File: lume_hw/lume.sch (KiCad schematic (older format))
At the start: 76 parts, among them SW1 BUTTON, SW2 BUTTON, SW3 BUTTON

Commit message: + Lume3 sent to production
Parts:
- removed DA1: AAT3221, symbol AAT3221
- removed DA2: NCP662SQ, symbol NCP662SQ
- removed DD1, DD3: PCA9635, symbol PCA9635
- removed DD2: STM32F100C4, symbol STM32F100C4
- removed FU1, FU2, FU3, FU4: SOLDERFUSE, symbol SOLDERFUSE
- removed HOLE1, HOLE2, HOLE3, HOLE4: HOLE_METALLED, symbol HOLE_METALLED-RESCUE-lume2
- removed R10, R11, R12, R13, R14, R15, R16, R17, R18, R19, R20, R21, R22, R23, R24, R25, R26, R27, R28, R29, R30, R31, R33, R4, R5, R6, R7, R8, R9: 100R, RES_0603, symbol R
- removed R32, R34: 4k7, RES_0603, symbol R
- removed XL1: CONN_3, symbol CONN_3
- removed XL10: CONN_1, symbol CONN_1
- removed XL2, XL4, XL5, XL6, XL7: CONN_10, symbol CONN_10
- removed XL9: USB_MINI_B, symbol USB_MINI_B
- added C14: 0.1u, Capacitors:CAP_0603, symbol C
- added DA1: NCP583SQ, SOT:SC82AB, symbol NCP583SQ
- added DA2: MCP1700, SOT:SOT23-3, symbol MCP1700
- added DA3: MC74VHC1, SOT:SOT23-5, symbol MC74VHC1
- added DD1: STM32F072CxTx, LQFP_TQFP:LQFP48, symbol STM32F072CxTx
- added HOLE1, HOLE2, HOLE3, HOLE4: HOLE_METALLED, PCB:Hole3_5_out6mm, symbol HOLE_METALLED
- added Logo1: Logo, Pictures:Ostranna_12d7_10d1, symbol Logo
- added Q1: ALS-PT19-315C, Resistors:RES_0603, symbol Phototransistor
- added SW4: BUTTON, BtnsSwitches:BTN_6x6_4x4, symbol BUTTON
- added TP1, TP2: TESTPOINT, PCB:TESTPOINT_1MM, symbol TESTPOINT
- added XL1: USB_MINI_B, Connectors:USBmicro_MOLEX_1050170001, symbol USB_MINI_B
- added XL2: CONN_6, Connectors:PLS-6, symbol CONN_6
- added XL4: CONN_3, Connectors:SLD_3_2D5, symbol CONN_3
- added XTAL2: 12MHz, Quartz:0503x4-4, symbol CRYSTAL_H
- B1: footprint CR2032 -> Installation:BATTERY_CH7410
- C1: value 4.7u -> 10n; footprint CAP_0603 -> Capacitors:CAP_0603
- C10: value 4.7u -> 6.8pF; footprint CAP_0603 -> Capacitors:CAP_0603; Price (none) -> 0.5; SolderPoints (none) -> 2
- C11: value 0.1u -> 18pF; footprint CAP_0603 -> Capacitors:CAP_0603; Price (none) -> 0.5; SolderPoints (none) -> 2
- C12: value 1u -> 18pF; footprint CAP_0603 -> Capacitors:CAP_0603; Price (none) -> 0.5; SolderPoints (none) -> 2
- C13: value 1u -> 0.1u; footprint CAP_0603 -> Capacitors:CAP_0603
- C2, C5: value 0.1u -> 1u; footprint CAP_0603 -> Capacitors:CAP_0603
- C3, C4, C9: footprint CAP_0603 -> Capacitors:CAP_0603; Price (none) -> 0.5; SolderPoints (none) -> 2
- C6: value 4.7u -> 0.1u; footprint CAP_0603 -> Capacitors:CAP_0603; Price (none) -> 0.5; SolderPoints (none) -> 2
- C7: value 1u -> 10u; footprint CAP_0603 -> Capacitors:CAP_0603; Price (none) -> 0.5; SolderPoints (none) -> 2
- C8: value 6.8pF -> 1u; footprint CAP_0603 -> Capacitors:CAP_0603; Price (none) -> 0.5; SolderPoints (none) -> 2
- D1: value SS14 -> PMEG2020; footprint SMA -> Diodes:SOD323; Price (none) -> 5; SolderPoints (none) -> 2
- R1: value 100R -> 1k; footprint RES_0603 -> Resistors:RES_0603; Price (none) -> 0.5; SolderPoints (none) -> 2
- R2: value 100R -> 10k; footprint RES_0603 -> Resistors:RES_0603; Price (none) -> 0.5; SolderPoints (none) -> 2
- R3: footprint RES_0603 -> Resistors:RES_0603; Price (none) -> 0.5; SolderPoints (none) -> 2
- SW1, SW2, SW3: footprint (none) -> BtnsSwitches:BTN_6x6_4x4; Price (none) -> 1; SolderPoints (none) -> 4
- XL3: footprint (none) -> Connectors:NOKIA_10PIN
- XL8: footprint (none) -> Connectors:SLD_2_2D5
- XTAL1: footprint (none) -> Quartz:KX26
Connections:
- net +3.3V: now also C8.1, DA1.3 (Vout), DA2.2 (OUT), DD1.24 (VDD), DD1.36 (VDD), DD1.48 (VDD), DD1.9 (VDDA), Q1.1 (C), XL2.1; no longer C1.1, C10.1, C11.1, C13.1, C2.1
- net +5V: now also C1.2, C2.1, C14.1, DA1.1 (EN), DA1.4 (Vin), DA2.3 (IN), DA3.5 (Vcc), XL1.1 (UVcc), XL4.1 (P1); no longer C12.1
- net Btn1: now also DD1.39 (PB3/T2C2/SCK1)
- net Btn2: now also DD1.40 (PB4/T3C1/MISO1)
- net Btn3: now also DD1.41 (PB5/T3C2/MOSI1)
- net GND: now also C1.1, R2.2, XL8.1 (P1), C14.2, DA1.2 (GND), DA2.1 (GND), DA3.1 (~OE), DA3.3 (GND), DD1.23 (VSS), DD1.35 (VSS), DD1.44 (BOOT0), DD1.47 (VSS), DD1.8 (VSSA), HOLE1.H, HOLE2.H, HOLE3.H, HOLE4.H, SW4.1, XL1.4 (UID), XL1.5 (UGND), XL2.3, XL4.3, XTAL2.H; no longer C1.2, XL8.2 (PM)
- net LCD_BCKLT: now also R3.1, DD1.27 (PB14/MISO2/SDA2/T1C2N/T15C1); no longer XL3.6 (LED+)
- net LCD_SCLK: now also DD1.25 (PB12/CK3)
- net LCD_SDA: now also DD1.21 (PB10/SCK2/SCL2/TX3/T2C3)
- net LCD_XCS: now also DD1.26 (PB13/SCK2/SCL2/T1C1N)
- net LCD_XRES: now also DD1.22 (PB11/SDA2/RX3/T2C4)
- net SWCLK: now also DD1.37 (TX2/SWCLK/PA14), XL2.2
- net SWDIO: now also DD1.34 (IROUT/USBNOE/SWDIO/PA13), XL2.4
- net at XTAL1.1: now also C10.1, DD1.3 (OC32IN/PC14); no longer C9.1
- net at XTAL1.2: now also C9.1, DD1.4 (OC32OUT/PC15); no longer C8.1
- net at B1.A: now also DD1.1 (VBat)
- net at R1.1: now also C11.1, XTAL2.2
- net LUM_MEAS: now reaches R2.1
- net LUM_MEAS: now also C13.1, DD1.11 (ADC1/RX4/T15C1N/T2C2/PA1), Q1.2 (E)
- net at R1.2: now also DD1.6 (OSCOUT/PF1)
- net at R3.2: now also XL3.6 (LED+)
- net at D1.A: now also XL8.2 (PM); no longer XL8.1 (P1)
- new net: DA3.4 (OutY), XL4.2 (PM)
- new net: C12.1, DD1.5 (OSCIN/PF0), XTAL2.1
- new net Btn4: DD1.42 (PB6/SCL1/T16C1N/TX1), SW4.2
- new net D+: DD1.33 (T1ETR/USBDP/PA12), XL1.3 (D+)
- new net D-: DD1.32 (T1C4/USBDM/PA11), XL1.2 (D-)
- new net MCO: DD1.29 (MCO/CK1/T1C1/PA8), TP1.1
- new net UART_RX: DD1.31 (T1C3/RX1/PA10), XL2.6
- new net UART_TX: DD1.30 (T1C2/TX1/PA9), XL2.5
- new net WS_CTRL: DA3.2 (InA), DD1.28 (PB15/MOSI2/T1C3N/T15C1N/T15C2), TP2.1
- no-connect marks 16 -> 20
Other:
- note added: "One or another"
- note added: "Programming & debug"
- note removed: "3.3V 150mA power regulator"
- note removed: "Address\nsetting"
- note removed: "LEDs controller\nI2C addr = 0x1A"
- note removed: "LEDs controller\nI2C addr = 0x2B"
- moved on the sheet: XL3, XTAL1

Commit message: proceeding
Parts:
- removed C11, C12: 18pF, Capacitors:CAP_0603, symbol C
- removed R1: 1k, Resistors:RES_0603, symbol R
- removed XTAL2: 12MHz, Quartz:0503x4-4, symbol CRYSTAL_H
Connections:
- no-connect marks 20 -> 22
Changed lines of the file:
@@
 	5900 3100 6350 3100
-$Comp
-L CONN_3 XL4
-U 1 1 59A0593F
-P 14700 3800
-F 0 "XL4" V 14650 3800 40  0000 C CNN
-F 1 "CONN_3" V 14750 3800 40  0000 C CNN
-F 2 "Connectors:SLD_3_2D5" V 14550 3700 60  0001 C CNN
-F 3 "" V 14650 3800 60  0001 C CNN
-F 4 "1" V 14750 3900 60  0001 C CNN "Price"
-F 5 "3" V 14850 4000 60  0001 C CNN "SolderPoints"
-	1    14700 3800
-	-1   0    0    -1
-$EndComp
 $Comp
 L +5V #PWR029
@@
 $EndComp
 NoConn ~ 9600 3500
-$Comp
-L GND #PWR020
-U 1 1 59A128EC
-P 10850 4800
-F 0 "#PWR020" H 10940 4780 30  0001 C CNN
-F 1 "GND" H 10850 4720 30  0001 C CNN
-F 2 "" H 10850 4800 60  0001 C CNN
-F 3 "" H 10850 4800 60  0001 C CNN
-	1    10850 4800
-	-1   0    0    -1
-$EndComp
-$Comp
-L GND #PWR022
-U 1 1 59A128F2
-P 11050 4800
-F 0 "#PWR022" H 11140 4780 30  0001 C CNN
-F 1 "GND" H 11050 4720 30  0001 C CNN
-F 2 "" H 11050 4800 60  0001 C CNN
-F 3 "" H 11050 4800 60  0001 C CNN
-	1    11050 4800
-	-1   0    0    -1
-$EndComp
-$Comp
-L GND #PWR019
-U 1 1 59A128F8
-P 10650 4800
-F 0 "#PWR019" H 10740 4780 30  0001 C CNN
-F 1 "GND" H 10650 4720 30  0001 C CNN
-F 2 "" H 10650 4800 60  0001 C CNN
-F 3 "" H 10650 4800 60  0001 C CNN
-	1    10650 4800
-	-1   0    0    -1
-$EndComp
-$Comp
-L R R1
-U 1 1 59A12900
-P 10650 3900
-F 0 "R1" V 10730 3750 50  0000 C CNN
-F 1 "1k" V 10650 3900 50  0000 C CNN
-F 2 "Resistors:RES_0603" V 10730 4000 28  0001 C CNN
-F 3 "" V 10730 3750 60  0000 C CNN
-F 4 "0.5" V 10830 3850 60  0001 C CNN "Price"
-F 5 "2" V 10930 3950 60  0001 C CNN "SolderPoints"
-	1    10650 3900
-	1    0    0    1
-$EndComp
-$Comp
-L CRYSTAL_H XTAL2
-U 1 1 59A12909
-P 10850 4250
-F 0 "XTAL2" V 10750 4500 60  0000 C CNN
-F 1 "12MHz" V 10850 4500 60  0000 C CNN
-F 2 "Quartz:0503x4-4" H 10875 4375 39  0001 C CNN
-F 3 "" H 10850 4525 60  0001 C CNN
-F 4 "15" H 10950 4625 60  0001 C CNN "Price"
-F 5 "4" H 11050 4725 60  0001 C CNN "SolderPoints"
-	1    10850 4250
-	-1   0    0    -1
-$EndComp
-$Comp
-L C C12
-U 1 1 59A12912
-P 11050 4550
-F 0 "C12" V 10950 4350 50  0000 L CNN
-F 1 "18pF" V 10950 4650 50  0000 L CNN
-F 2 "Capacitors:CAP_0603" V 11150 4400 28  0001 C BNN
-F 3 "" H 10950 4450 60  0001 C CNN
-F 4 "0.5" H 11050 4550 60  0001 C CNN "Price"
-F 5 "2" H 11150 4650 60  0001 C CNN "SolderPoints"
-	1    11050 4550
-	-1   0    0    -1
-$EndComp
-$Comp
-L C C11
-U 1 1 59A1291B
-P 10650 4550
-F 0 "C11" V 10550 4350 50  0000 L CNN
-F 1 "18pF" V 10550 4650 50  0000 L CNN
-F 2 "Capacitors:CAP_0603" V 10750 4400 28  0001 C BNN
-F 3 "" H 10550 4450 60  0001 C CNN
-F 4 "0.5" H 10650 4550 60  0001 C CNN "Price"
-F 5 "2" H 10750 4650 60  0001 C CNN "SolderPoints"
-	1    10650 4550
-	1    0    0    -1
-$EndComp
-Wire Wire Line
-	11000 4250 11050 4250
-Wire Wire Line
-	11050 3250 11050 4350
-Wire Wire Line
-	10650 4350 10650 4150
-Wire Wire Line
-	10650 4250 10700 4250
-Connection ~ 10650 4250
-Connection ~ 11050 4250
-Wire Wire Line
-	11050 4800 11050 4750
-Wire Wire Line
-	10650 4750 10650 4800
-Wire Wire Line
-	10850 4800 10850 4400
-Wire Wire Line
-	9600 3350 10650 3350
-Wire Wire Line
-	10650 3350 10650 3650
-Wire Wire Line
-	9600 3250 11050 3250
 NoConn ~ 9600 3100
 NoConn ~ 6350 1600
@@
 	1    0    0    -1
 $EndComp
+$Comp
+L CONN_3 XL4
+U 1 1 59A0593F
+P 14700 3800
+F 0 "XL4" V 14650 3800 40  0000 C CNN
+F 1 "CONN_3" V 14750 3800 40  0000 C CNN
+F 2 "Connectors:SLD_3_2D5" V 14550 3700 60  0001 C CNN
+F 3 "" V 14650 3800 60  0001 C CNN
+F 4 "1" V 14750 3900 60  0001 C CNN "Price"
+F 5 "3" V 14850 4000 60  0001 C CNN "SolderPoints"
+	1    14700 3800
+	-1   0    0    -1
+$EndComp
+NoConn ~ 9600 3250
+NoConn ~ 9600 3350
 $EndSCHEMATC

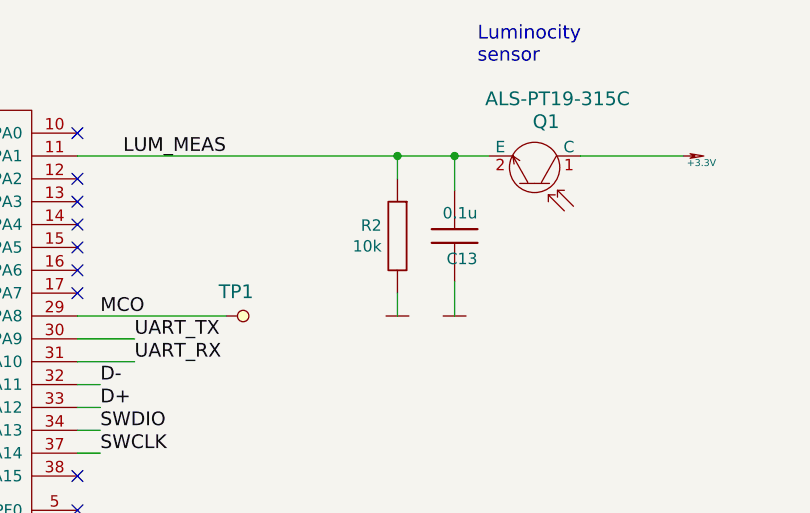
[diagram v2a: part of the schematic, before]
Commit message: + WS2812 LEDs * Sch: 100k instead of 10k at light sns
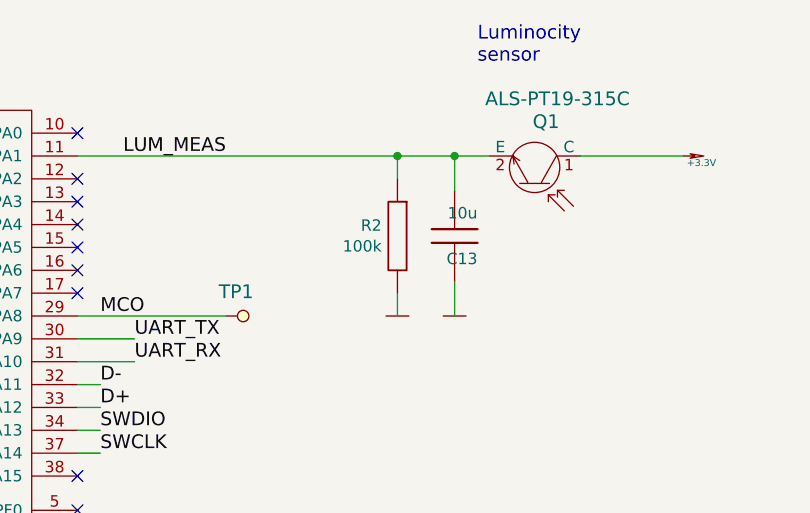
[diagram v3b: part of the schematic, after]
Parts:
- C13: value 0.1u -> 10u
- R2: value 10k -> 100k
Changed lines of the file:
@@
 P 11250 2050
 F 0 "C13" H 11150 1950 50  0000 L CNN
-F 1 "0.1u" H 11150 2150 50  0000 L CNN
+F 1 "10u" H 11150 2150 50  0000 L CNN
 F 2 "Capacitors:CAP_0603" V 11350 1900 28  0001 C BNN
 F 3 "" H 11250 2050 60  0001 C CNN
@@
 P 11000 2050
 F 0 "R2" H 11069 2096 50  0000 L CNN
-F 1 "10k" H 11069 2005 50  0000 L CNN
+F 1 "100k" H 11069 2005 50  0000 L CNN
 F 2 "Resistors:RES_0603" V 11080 2150 28  0001 C CNN
 F 3 "" V 11080 1900 60  0000 C CNN

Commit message: + ADC tested * Luminocity sensor sch changed + New PCB sent to production
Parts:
- added C11: 0.1u, Capacitors:CAP_0603, symbol C
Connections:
- net +3.3V: no longer XL3.10 (VDDI), XL3.9 (VDD)
- net GND: now also C11.2
- net LCD_PWR: now reaches DD1.16 (ADC6/T16C1/T3C1/MISO1/PA6)
- net LCD_PWR: now also XL3.10 (VDDI), XL3.9 (VDD), C11.1
- no-connect marks 22 -> 21
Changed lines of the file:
@@
 Connection ~ 1800 3900
 Wire Wire Line
-	1800 3900 1950 3900
+	1800 3900 2700 3900
 Wire Wire Line
 	1750 3950 1800 3950
@@
 	0    -1   -1   0
 $EndComp
-$Comp
-L +3.3V #PWR09
-U 1 1 505F2C93
-P 1950 3900
-F 0 "#PWR09" H 1950 3860 30  0001 C CNN
-F 1 "+3.3V" H 2030 3930 30  0000 C CNN
-F 2 "" H 1950 3900 60  0001 C CNN
-F 3 "" H 1950 3900 60  0001 C CNN
-	1    1950 3900
-	1    0    0    -1
-$EndComp
 Text Notes 850  3900 0    60   ~ 0
 LCD
@@
 NoConn ~ 9600 2000
 NoConn ~ 9600 2100
-NoConn ~ 9600 2200
 NoConn ~ 9600 2300
 $Comp
@@
 NoConn ~ 9600 3250
 NoConn ~ 9600 3350
+Text Label 2700 3900 0    60   ~ 0
+LCD_PWR
+Text Label 9700 2200 0    60   ~ 0
+LCD_PWR
+Wire Wire Line
+	9700 2200 9600 2200
+Wire Wire Line
+	2500 3350 2500 3250
+$Comp
+L GND #PWR09
+U 1 1 59C0368E
+P 2500 3250
+F 0 "#PWR09" H 2590 3230 30  0001 C CNN
+F 1 "GND" H 2500 3170 30  0001 C CNN
+F 2 "" H 2500 3250 60  0001 C CNN
+F 3 "" H 2500 3250 60  0001 C CNN
+	1    2500 3250
+	1    0    0    1
+$EndComp
+$Comp
+L C C11
+U 1 1 59C03696
+P 2500 3550
+F 0 "C11" H 2400 3650 50  0000 L CNN
+F 1 "0.1u" H 2400 3450 50  0000 L CNN
+F 2 "Capacitors:CAP_0603" V 2600 3400 28  0001 C BNN
+F 3 "" H 2400 3450 60  0001 C CNN
+F 4 "0.5" H 2500 3550 60  0001 C CNN "Price"
+F 5 "2" H 2600 3650 60  0001 C CNN "SolderPoints"
+	1    2500 3550
+	1    0    0    1
+$EndComp
+Wire Wire Line
+	2500 3750 2500 3900
+Connection ~ 2500 3900
 $EndSCHEMATC
